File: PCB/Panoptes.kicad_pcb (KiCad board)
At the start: 4 copper layers, 125.5 x 104.5 mm, 114 parts, among them J1 Conn_01x02, J2 Conn_02x06_Odd_Even, J3 Conn_02x12_Odd_Even, J4 Conn_01x04, J5 Conn_01x02, J6 Conn_01x02, Q1 2N2222AUB, U1 SK0530, U2 SE555D, U3 ADS7882, U4 ARS14Y03, U5 OPA2350UA, U6 L79L05_SOT89, U7 OPA2350UA, U8 L78L33_SOT89, U9 L78L05_SOT89

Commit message: start of rev.3
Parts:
- C14, C16, C18: footprint Capacitor_SMD:C_1206_3216Metric -> Capacitor_SMD:C_1812_4532Metric
- J5: value Conn_01x02 -> Conn_01x05; footprint Connector_PinHeader_2.54mm:PinHeader_1x02_P2.54mm_Vertical -> Connector_PinHeader_2.54mm:PinHeader_1x05_P2.54mm_Vertical
- TP2: renamed from TP10; value HV Prog -> HV prog
- moved J6 62.3 mm to (112.2, 117.5), turned to 0 degrees
- moved J5 0.67 mm to (98.9, 55.2)
- moved U6 0.35 mm to (98.2, 64.0)
- moved U8 0.10 mm to (119.8, 64.5)
- moved U9 0.10 mm to (107.5, 64.2)
- renumbered TP12 to TP1, TP8 to TP10, TP4 to TP11, TP5 to TP12, TP9 to TP13, TP13 to TP3, TP11 to TP4, TP6 to TP5, TP1 to TP6, TP2 to TP7, TP7 to TP8, TP3 to TP9
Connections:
- J5 pad 1: -9V -> +9V
- J5 pad 2: GND -> -9V
- J6 pad 1: +9V -> +5V
- J6 pad 2: GND -> /HV_+5V
- R2 pad 1: +5V -> /HV_+5V
- U1 pad 1: +5V -> /HV_+5V
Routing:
- net /HV_+5V: track 0.00 -> 28.9 mm
- net +5V: track 31.0 -> 16.5 mm
- net Net-(C14-Pad2): track 9.80 -> 8.65 mm
- net Net-(C16-Pad2): track 9.80 -> 8.65 mm
- net /Vbias: track 17.5 -> 16.9 mm
- net GND: vias 606 -> 740
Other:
- board size 125.5 x 104.5 mm -> 237.2 x 124.5 mm
- board text added: "HV Enable"

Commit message: All signals routed
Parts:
- removed the C18 at (69.0, 108.0)
- removed H1, H2, H3, H4: MountingHole_Pad, MountingHole:MountingHole_4mm_Pad_Via
- removed the R13 at (130.0, 71.2)
- removed the R16 at (130.0, 74.5)
- removed the R2 at (99.8, 105.0)
- removed the R21 at (150.8, 68.0)
- removed the R24 at (150.8, 71.2)
- removed R28, R33: 10k, Resistor_SMD:R_1206_3216Metric
- removed R29, R31: 1k, Resistor_SMD:R_1206_3216Metric
- removed the R3 at (105.5, 105.0)
- removed the R8 at (130.0, 68.0)
- removed the TP4 at (77.0, 145.2)
- removed the U1 at (81.1, 151.6)
- removed the U4 at (81.8, 93.2)
- removed the U5 at (106.8, 93.8)
- added J1: Conn_02x05_Odd_Even, Connector_PinSocket_2.54mm:PinSocket_2x05_P2.54mm_Horizontal, F.Cu at (195.9, 37.8)
- added R27: 100, Resistor_SMD:R_1206_3216Metric, F.Cu at (240.8, 93.5)
- added RV1: 20k, Panoptes:Bourns 3361P, F.Cu at (191.0, 95.2)
- added RV2: 2k, Panoptes:Bourns 3361P, F.Cu at (190.5, 77.2)
- added RV3: 2k, Panoptes:Bourns 3361P, F.Cu at (216.2, 93.0)
- added RV4: 20k, Panoptes:Bourns 3361P, F.Cu at (190.5, 86.2)
- added RV5: 20k, Panoptes:Bourns 3361P, F.Cu at (216.2, 78.0)
- added RV6: 10k, Panoptes:Bourns 3361P, F.Cu at (247.8, 95.0)
- added U6: OPA2350UA, Package_SO:SOIC-8_3.9x4.9mm_P1.27mm, F.Cu at (205.5, 84.8)
- added U8: SK0530, Panoptes:SK0530, F.Cu at (244.0, 145.8)
- C37: renamed from C14; footprint Capacitor_SMD:C_1812_4532Metric -> Capacitor_THT:C_Disc_D10.5mm_W5.0mm_P7.50mm
- C38: renamed from C16; footprint Capacitor_SMD:C_1812_4532Metric -> Capacitor_THT:C_Disc_D10.5mm_W5.0mm_P7.50mm
- J2: value Conn_02x06_Odd_Even -> Conn_02x10_Odd_Even; footprint Connector_PinHeader_2.54mm:PinHeader_2x06_P2.54mm_Vertical -> Connector_PinSocket_2.54mm:PinSocket_2x10_P2.54mm_Horizontal
- J3: value Conn_02x12_Odd_Even -> Conn_01x02; footprint Connector_PinHeader_2.54mm:PinHeader_2x12_P2.54mm_Vertical -> Connector_PinSocket_2.54mm:PinSocket_1x02_P2.54mm_Horizontal
- J4: value Conn_01x04 -> Conn_01x03; footprint Connector_PinHeader_2.54mm:PinHeader_1x04_P2.54mm_Vertical -> Panoptes:STX-3500-3NTR
- J5: value Conn_01x05 -> Conn_01x03; footprint Connector_PinHeader_2.54mm:PinHeader_1x05_P2.54mm_Vertical -> Connector_PinHeader_2.54mm:PinHeader_1x03_P2.54mm_Vertical
- Q1: value 2N2222AUB -> MMBT3904; footprint Panoptes:2N2222AUB -> Package_TO_SOT_SMD:SOT-23-3
- TP1: renamed from TP3; value Pulse out -> P_out
- TP10: renamed from TP7; value Amp2 Out -> A2_Out
- TP11: renamed from TP2; value HV prog -> HV_prog
- TP2: renamed from TP1; value Pulse Trig -> P_Trig
- TP6: value Amp1 Out -> A1_Out
- TP7: renamed from TP9; value Amp3 Out -> A3_Out
- TP8: renamed from TP5; value Test Pulse -> Test_P
- moved TP8 188.3 mm to (259.0, 85.5)
- moved C1 188.3 mm to (269.0, 74.0)
- moved C13 188.3 mm to (257.0, 74.0)
- moved C14 188.3 mm to (266.2, 80.5)
- moved C15 188.3 mm to (260.5, 77.2)
- moved C16 188.3 mm to (260.5, 80.5)
- moved C2 188.3 mm to (269.0, 70.8)
- moved C3 188.3 mm to (256.2, 84.0)
- moved C4 188.3 mm to (253.0, 84.0)
- moved C5 188.3 mm to (249.8, 84.0)
- moved C6 188.3 mm to (246.5, 84.0)
- moved C7 188.3 mm to (243.2, 84.0)
- moved C8 188.3 mm to (240.0, 84.0)
- moved Q1 188.3 mm to (263.8, 63.8), turned to -90 degrees
- moved R1 188.3 mm to (249.8, 63.8)
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- renumbered C5 to C1, C3 to C10, C6 to C11, C10 to C12, C15 to C14, C17 to C15, C19 to C16, C7 to C17, C11 to C18, C25 to C19, C9 to C2, C28 to C20, C30 to C21, C2 to C22, C4 to C23, C8 to C24, C12 to C25, C32 to C26, C34 to C27, C37 to C28, C39 to C29, C20 to C3, C40 to C30, C41 to C31, C21 to C32, C23 to C33, C26 to C34, C38 to C35, C22 to C4, C33 to C40, C35 to C41, C24 to C5, C27 to C6, C29 to C7, C31 to C8, C1 to C9, J1 to J6, J6 to J7, R9 to R1, R12 to R10, R19 to R11, R14 to R12, R1 to R13, R30 to R14, R34 to R15, R37 to R16, R22 to R17, R20 to R18, R25 to R19, R15 to R2, R23 to R20, R32 to R21, R35 to R22, R36 to R23, R27 to R24, R6 to R25, R10 to R3, R17 to R4, R4 to R5, R5 to R6, R11 to R7, R7 to R8, R18 to R9, TP8 to TP3, TP10 to TP4, TP13 to TP5, TP11 to TP9, U2 to U1, U3 to U2, U6 to U3, U8 to U4, U9 to U5
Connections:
- C35 pad 1: Net-(C36-Pad1) -> /B_out_4
- C35 pad 2: /B_out_4 -> Net-(C35-Pad2)
- C36 pad 1: Net-(C36-Pad1) -> /B_out_4
- C36 pad 2: /B_out_4 -> Net-(C35-Pad2)
- C38 pad 2: Net-(C16-Pad2) -> /NC
- C40 pad 1: /B+4 -> Net-(U6B-B+)
- C41 pad 1: /B+4 -> Net-(U6B-B+)
- J2 pad 1: /~CS -> GND
- J2 pad 10: GND -> /DB9
- J2 pad 11: /BUSY -> /DB2
- J2 pad 12: GND -> /DB8
- J2 pad 3: /~RD -> /DB5
- J2 pad 4: GND -> /DB11
- J2 pad 5: /~CONVST -> /DB4
- J2 pad 6: GND -> /DB10
- J2 pad 7: /~PWD_RST -> GND
- J2 pad 9: /~A_PWD -> /DB3
- J3 pad 1: /DB0 -> /TR
- J4 pad 1: /coil+ -> -9V
- J4 pad 2: GND -> +9V
- J4 pad 3: /TR -> GND
- J5 pad 1: +9V -> /NO
- J5 pad 2: -9V -> /COM
- J5 pad 3: GND -> /NC
- R21 pad 1: /B-4 -> Net-(U6B-B-)
- R24 pad 2: /A-3 -> Net-(U6A-A-)
- R26 pad 1: /B_out_2 -> /HV_+5V
- R26 pad 2: /B-2 -> /Vprogram
- U7 pad 1: /A_out_3 -> /A_out_1
- U7 pad 2: /A-3 -> /COM
- U7 pad 3: /B_out_2 -> GND
- U7 pad 5: /B+4 -> GND
- U7 pad 6: /B-4 -> /B-2
- U7 pad 7: /B_out_4 -> /B_out_2
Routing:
- net GND: track 203.4 -> 70.7 mm, vias 740 -> 241
- net /TR: track 5.46 -> 47.5 mm
- net +5V: track 16.5 -> 52.5 mm, vias 30 -> 10
- net /NO: track 26.4 -> 61.3 mm
- net /coil+: track 32.9 -> 0.00 mm
- net Net-(C35-Pad2): track 0.00 -> 31.5 mm, vias 0 -> 2
- net /DB0: track 39.7 -> 21.4 mm
- net /DB1: track 39.7 -> 22.3 mm
- net /HV: track 32.6 -> 16.0 mm
- net Net-(C36-Pad1): track 16.3 -> 0.00 mm
- net /B_out_4: track 18.4 -> 34.3 mm
- net /DB2: track 39.7 -> 24.2 mm
- net +9V: track 0.00 -> 15.3 mm
- net Net-(U6A-A-): track 0.00 -> 15.3 mm
- net /A_out_1: track 30.0 -> 15.2 mm, vias 2 -> 0
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- removed copper zone on B.Cu, net +3V3
- removed copper zone on F.Cu, net +3V3
- removed copper zone on B.Cu, net +5V
- removed copper zone on F.Cu, net +5V
- removed copper zone on F.Cu, net +9V
- removed copper zone on B.Cu, net -5V
- removed copper zone on F.Cu, net -5V
- removed copper zone on F.Cu, net -9V
- removed copper zone on F.Cu, net /B+4
- removed copper zone on F.Cu, net /Vbias
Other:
- board size 237.2 x 124.5 mm -> 100 x 120 mm
- board text added: "D0/D06"
- board text added: "D1/D07"
- board text added: "D2/D08"
- board text added: "D3/D09"
- board text added: "D4/D10"
- board text added: "D5/D11"
- board text added: "GND"
- board text added: "Panoptes V3"
- board text added: "~{CONVST} / BUSY"
- board text added: "~{CS} / ~{PWD_RST}"
- board text added: "~{RD} / ~{A_PWD}"
- board text removed: "+9V"
- board text removed: "-9V"
- board text removed: "BUSY"
- board text removed: "COIL"
- board text removed: "D00"
- board text removed: "D01"
- board text removed: "D02"
- board text removed: "D03"
- board text removed: "D04"
- board text removed: "D05"
- board text removed: "D06"
- board text removed: "D07"
- board text removed: "D08"
- board text removed: "D09"
- board text removed: "D10"
- board text removed: "D11"
- board text removed: "Panoptes V2.5"
- board text removed: "TR"
- board text removed: "~A_PWD"
- board text removed: "~CONVST"
- board text removed: "~CS"
- board text removed: "~PWD_RST"
- board text removed: "~RD"

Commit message: V3 completed
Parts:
- added R23: 500M, Resistor_THT:R_Axial_DIN0207_L6.3mm_D2.5mm_P7.62mm_Horizontal, F.Cu at (85.5, 138.0)
- added R24: 500M, Resistor_THT:R_Axial_DIN0207_L6.3mm_D2.5mm_P7.62mm_Horizontal, F.Cu at (85.5, 124.1)
- added R25: 500M, Resistor_THT:R_Axial_DIN0207_L6.3mm_D2.5mm_P7.62mm_Horizontal, F.Cu at (85.5, 113.6)
- added R29: 1k5, Resistor_SMD:R_1206_3216Metric, F.Cu at (81.2, 112.8)
- added R30: 1M5, Resistor_SMD:R_1206_3216Metric, F.Cu at (81.2, 107.2)
- added TP10: HV_measure, TestPoint:TestPoint_Pad_D1.0mm, F.Cu at (85.5, 102.5)
- TP1, TP2, TP3, TP4, TP5, TP6, TP7, TP8, TP9: footprint TestPoint:TestPoint_Pad_D1.0mm -> Connector_PinHeader_2.54mm:PinHeader_1x01_P2.54mm_Vertical
- TP12: renamed from TP10; footprint TestPoint:TestPoint_Pad_D1.0mm -> Connector_PinHeader_2.54mm:PinHeader_1x01_P2.54mm_Vertical
- TP13: renamed from TP12; footprint TestPoint:TestPoint_Pad_D1.0mm -> Connector_PinHeader_2.54mm:PinHeader_1x01_P2.54mm_Vertical
- U6, U7: value OPA2350UA -> opa2727; footprint Package_SO:SOIC-8_3.9x4.9mm_P1.27mm -> Package_DFN_QFN:DFN-8-1EP_3x3mm_P0.65mm_EP1.55x2.4mm
- moved TP4 176.3 mm to (97.8, 39.2)
- moved D2 173.7 mm to (97.8, 34.5), turned to -90 degrees
- moved R15 172.6 mm to (94.8, 35.0), turned to 90 degrees
- moved C29 171.5 mm to (102.2, 36.3)
- moved R13 168.6 mm to (100.8, 57.2), turned to 0 degrees
- moved TP1 162.7 mm to (98.8, 68.0)
- moved C28 162.2 mm to (107.0, 40.2), turned to 180 degrees
- moved U4 159.6 mm to (106.8, 35.5), turned to 90 degrees
- moved TP9 157.0 mm to (44.5, 72.0)
- moved C30 156.8 mm to (107.0, 43.2), turned to 180 degrees
- moved U7 156.6 mm to (50.4, 84.1)
- moved R16 155.8 mm to (102.5, 52.5), turned to -90 degrees
- moved C1 155.5 mm to (66.8, 68.0)
- moved C10 155.5 mm to (97.5, 82.5)
- moved C11 155.5 mm to (94.2, 82.5)
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- renumbered C9 to C1, C4 to C10, C5 to C11, C6 to C12, C7 to C13, C8 to C14, C19 to C15, C20 to C16, C21 to C17, C13 to C18, C22 to C19, C10 to C2, C23 to C20, C24 to C21, C25 to C22, C14 to C23, C15 to C24, C16 to C25, C11 to C3, C37 to C36, C38 to C37, C36 to C38, C40 to C39, C12 to C4, C41 to C40, C1 to C5, C2 to C6, C17 to C7, C18 to C8, C3 to C9, J6 to J3, J5 to J4, J7 to J5, J3 to J6, J4 to J7, R25 to R21, R26 to R22, R21 to R26, R22 to R27, R23 to R28, R24 to R31, R27 to R32, RV6 to RV5, RV5 to RV6
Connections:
- C39 pad 1: Net-(U6B-B+) -> Net-(U7B-B+)
- C40 pad 1: Net-(U6B-B+) -> Net-(U7B-B+)
- R26 pad 1: Net-(U6B-B-) -> Net-(U7B-B-)
- R31 pad 2: Net-(U6A-A-) -> Net-(U7A-A-)
- RV3 pad 1: Net-(U6B-B+) -> Net-(U7B-B+)
- RV4 pad 2: Net-(U6A-A-) -> Net-(U7A-A-)
- RV6 pad 2: Net-(U6B-B-) -> Net-(U7B-B-)
- U6 pad 1: /A_out_3 -> /A_out_1
- U6 pad 2: Net-(U6A-A-) -> /COM
- U6 pad 3: /B_out_2 -> GND
- U6 pad 5: Net-(U6B-B+) -> GND
- U6 pad 6: Net-(U6B-B-) -> /B-2
- U6 pad 7: /B_out_4 -> /B_out_2
- U7 pad 1: /A_out_1 -> /A_out_3
- U7 pad 2: /COM -> Net-(U7A-A-)
- U7 pad 3: GND -> /B_out_2
- U7 pad 5: GND -> Net-(U7B-B+)
- U7 pad 6: /B-2 -> Net-(U7B-B-)
- U7 pad 7: /B_out_2 -> /B_out_4
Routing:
- net +5V: track 52.5 -> 234.0 mm, vias 10 -> 17
- net -5V: track 3.49 -> 97.8 mm, vias 2 -> 3
- net +3V3: track 10.0 -> 89.1 mm, vias 1 -> 3
- net GND: track 70.7 -> 95.9 mm, vias 241 -> 396
- net /TR: track 47.5 -> 30.4 mm
- net Net-(U7B-B-): track 0.00 -> 16.3 mm
- net Net-(U6A-A-): track 15.3 -> 0.00 mm
- net /A_out_1: track 15.2 -> 29.7 mm, vias 0 -> 2
- net Net-(U7A-A-): track 0.00 -> 13.1 mm
- net -9V: track 13.2 -> 25.5 mm
- net Net-(U6B-B-): track 12.3 -> 0.00 mm
- net Net-(U6B-B+): track 12.2 -> 0.00 mm
- net Net-(U7B-B+): track 0.00 -> 10.7 mm
- net /B-2: track 23.8 -> 34.4 mm, vias 0 -> 2
- net Net-(C35-Pad2): track 31.5 -> 41.4 mm
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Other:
- outline, holes or cut-outs redrawn
- board text added: "D00/D06"
- board text added: "D01/D07"
- board text added: "D02/D08"
- board text added: "D03/D09"
- board text added: "D04/D10"
- board text added: "D05/D11"
- board text added: "GND/GND"
- board text added: "Trigger"
- board text added: "~{CONVST}/BUSY"
- board text added: "~{CS}/~{PWD_RST}"
- board text added: "~{RD}/~{A_PWD}"
- board text removed: "D0/D06"
- board text removed: "D1/D07"
- board text removed: "D2/D08"
- board text removed: "D3/D09"
- board text removed: "D4/D10"
- board text removed: "D5/D11"
- board text removed: "~{CONVST} / BUSY"
- board text removed: "~{CS} / ~{PWD_RST}"
- board text removed: "~{RD} / ~{A_PWD}"

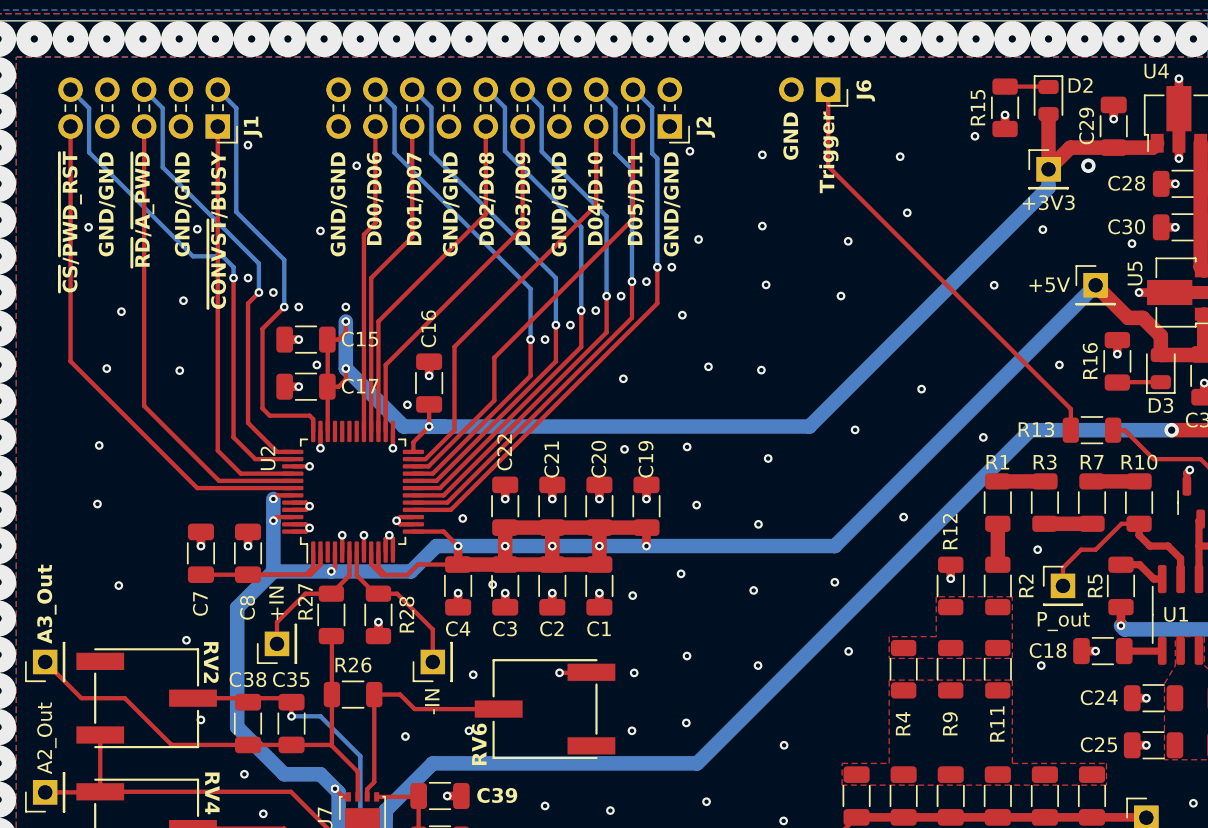
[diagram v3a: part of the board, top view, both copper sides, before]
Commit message: Added DNP cap to ADC input.
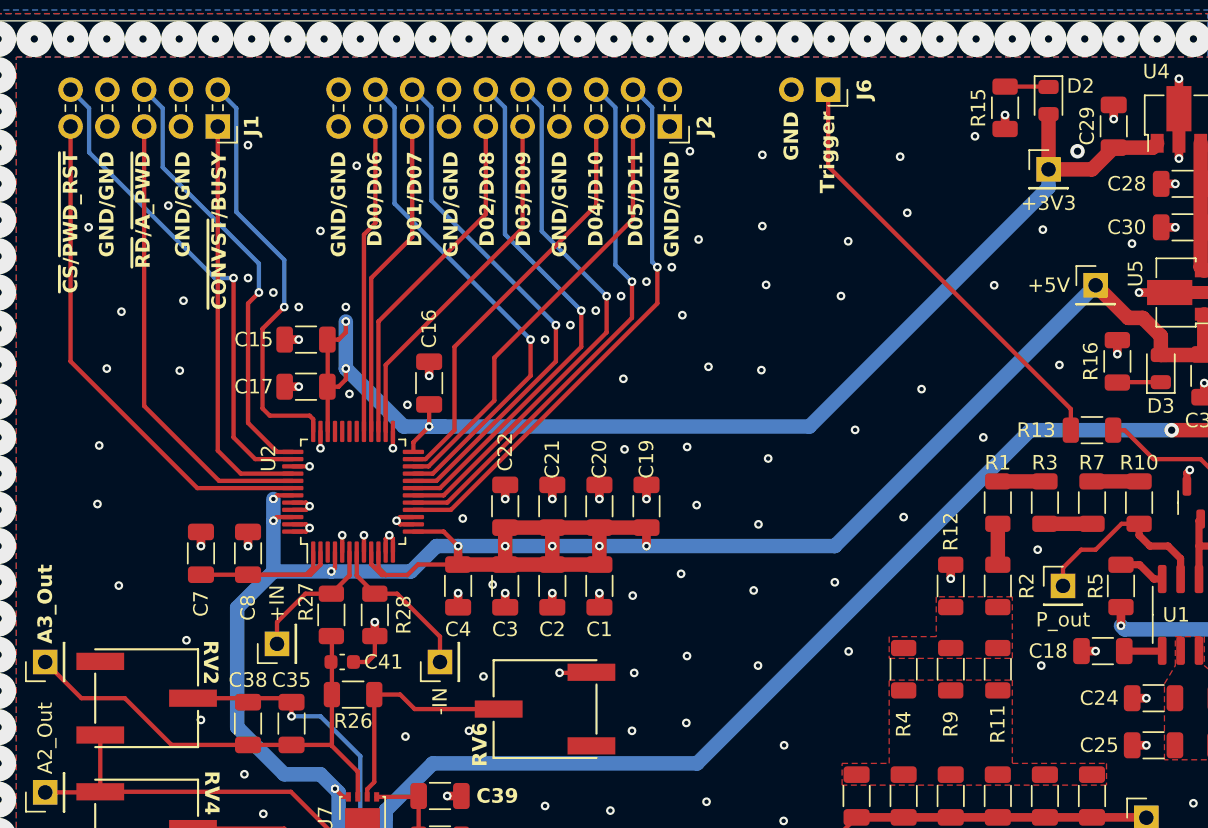
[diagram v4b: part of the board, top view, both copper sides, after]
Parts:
- added C41: 150p, Capacitor_SMD:C_0603_1608Metric, F.Cu at (49.0, 73.2)
- moved TP13 0.50 mm to (55.8, 73.2)
- moved R28 0.25 mm to (51.2, 70.0)
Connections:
- net /B_out_4 renamed /A_out
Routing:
- net GND: track 95.9 -> 98.9 mm
